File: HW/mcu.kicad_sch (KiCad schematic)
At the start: 10 parts, among them J2 JTAG, SW2 SW_DPST, SW3 SW_DPST, U1 ESP32-S2-MINI-2

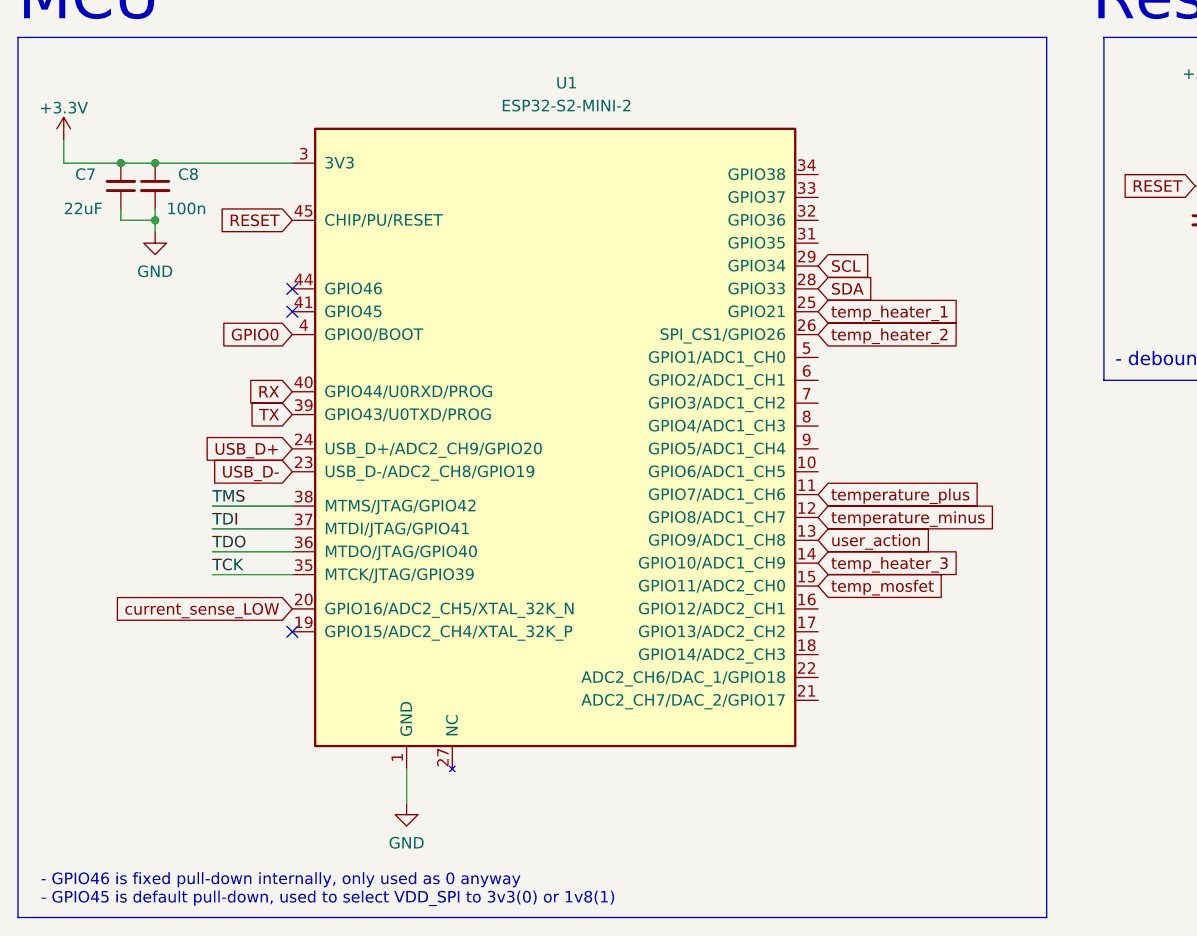
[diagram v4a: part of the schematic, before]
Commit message: starterd routing, removed OTG usb port
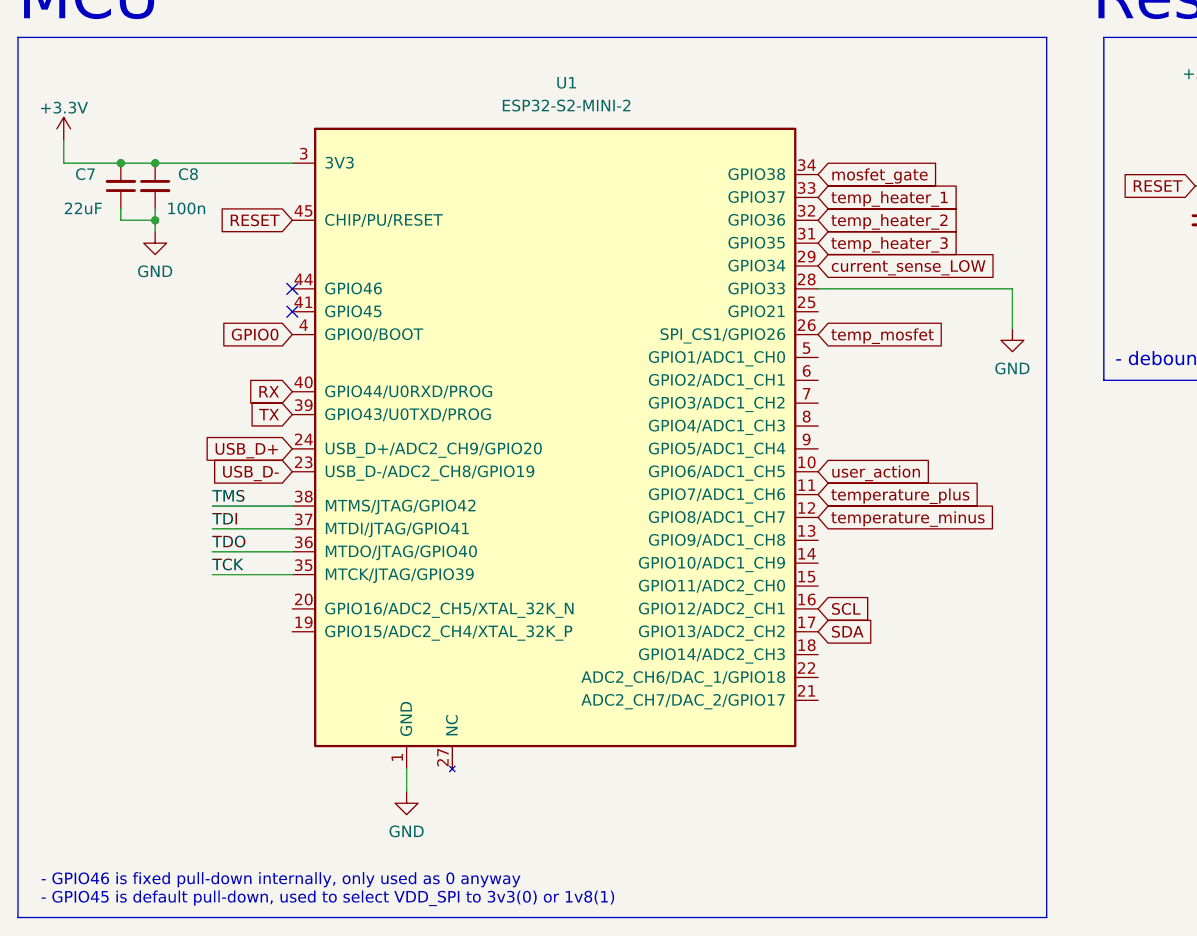
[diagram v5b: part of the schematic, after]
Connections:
- net GND: now also U1.2 (GND), U1.28 (GPIO33), U1.30 (GND), U1.42 (GND), U1.43 (GND), U1.46 (GND), U1.47 (GND), U1.48 (GND), U1.49 (GND), U1.50 (GND), U1.51 (GND), U1.52 (GND), U1.53 (GND), U1.54 (GND), U1.55 (GND), U1.56 (GND), U1.57 (GND), U1.58 (GND), U1.59 (GND), U1.60 (GND), U1.61 (GND), U1.62 (GND), U1.63 (GND), U1.64 (GND), U1.65 (GND)
- net SCL: now also U1.16 (GPIO12/ADC2_CH1); no longer U1.29 (GPIO34)
- net SDA: now also U1.17 (GPIO13/ADC2_CH2); no longer U1.28 (GPIO33)
- net current_sense_LOW: now also U1.29 (GPIO34); no longer U1.20 (GPIO16/ADC2_CH5/XTAL_32K_N)
- net temp_heater_1: now also U1.33 (GPIO37); no longer U1.25 (GPIO21)
- net temp_heater_2: now also U1.32 (GPIO36); no longer U1.26 (SPI_CS1/GPIO26)
- net temp_heater_3: now also U1.31 (GPIO35); no longer U1.14 (GPIO10/ADC1_CH9)
- net temp_mosfet: now also U1.26 (SPI_CS1/GPIO26); no longer U1.15 (GPIO11/ADC2_CH0)
- net user_action: now also U1.10 (GPIO6/ADC1_CH5); no longer U1.13 (GPIO9/ADC1_CH8)
- net mosfet_gate: now reaches U1.34 (GPIO38)
- no-connect marks 3 -> 2
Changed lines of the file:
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@@
   (no_connect (at 48.26 54.61))
   (no_connect (at 48.26 52.07))
-  (no_connect (at 48.26 90.17))
-  (wire (pts (xy 60.96 105.41) (xy 60.96 109.22))
+  (wire (pts (xy 60.96 105.41) (xy 60.96 107.95))
     (stroke (width 0) (type default) (color 0 0 0 0))
   )
@@
     (stroke (width 0) (type default) (color 0 0 0 0))
   )
+  (wire (pts (xy 106.68 52.07) (xy 128.27 52.07))
+    (stroke (width 0) (type default) (color 0 0 0 0))
+  )
   (wire (pts (xy 149.86 40.64) (xy 149.86 41.91))
     (stroke (width 0) (type default) (color 0 0 0 0))
@@
   )
   (wire (pts (xy 163.83 35.56) (xy 161.29 35.56))
+    (stroke (width 0) (type default) (color 0 0 0 0))
+  )
+  (wire (pts (xy 128.27 52.07) (xy 128.27 56.515))
     (stroke (width 0) (type default) (color 0 0 0 0))
   )
@@
     (effects (font (size 1.27 1.27)) (justify left bottom))
   )
-  (global_label "temp_heater_3" (shape input) (at 106.68 82.55 0) (fields_autoplaced)
-    (effects (font (size 1.27 1.27)) (justify left))
-    (property "Intersheet References" "${INTERSHEET_REFS}" (id 0) (at 122.8817 82.6294 0)
+  (global_label "temp_heater_3" (shape input) (at 106.68 46.99 0) (fields_autoplaced)
+    (effects (font (size 1.27 1.27)) (justify left))
+    (property "Intersheet References" "${INTERSHEET_REFS}" (id 0) (at 122.8817 47.0694 0)
       (effects (font (size 1.27 1.27)) (justify left) hide)
     )
@@
     )
   )
-  (global_label "user_action" (shape input) (at 106.68 80.01 0) (fields_autoplaced)
-    (effects (font (size 1.27 1.27)) (justify left))
-    (property "Intersheet References" "${INTERSHEET_REFS}" (id 0) (at 119.9788 80.0894 0)
+  (global_label "user_action" (shape input) (at 106.68 72.39 0) (fields_autoplaced)
+    (effects (font (size 1.27 1.27)) (justify left))
+    (property "Intersheet References" "${INTERSHEET_REFS}" (id 0) (at 119.9788 72.4694 0)
       (effects (font (size 1.27 1.27)) (justify left) hide)
     )
@@
     )
   )
-  (global_label "SDA" (shape input) (at 106.68 52.07 0) (fields_autoplaced)
-    (effects (font (size 1.27 1.27)) (justify left))
-    (property "Intersheet References" "${INTERSHEET_REFS}" (id 0) (at 112.6612 51.9906 0)
+  (global_label "SDA" (shape input) (at 106.68 90.17 0) (fields_autoplaced)
+    (effects (font (size 1.27 1.27)) (justify left))
+    (property "Intersheet References" "${INTERSHEET_REFS}" (id 0) (at 112.6612 90.0906 0)
       (effects (font (size 1.27 1.27)) (justify left) hide)
     )
@@
     )
   )
-  (global_label "temp_heater_1" (shape input) (at 106.68 54.61 0) (fields_autoplaced)
-    (effects (font (size 1.27 1.27)) (justify left))
-    (property "Intersheet References" "${INTERSHEET_REFS}" (id 0) (at 122.8817 54.6894 0)
-      (effects (font (size 1.27 1.27)) (justify left) hide)
-    )
-  )
-  (global_label "current_sense_LOW" (shape input) (at 48.26 87.63 180) (fields_autoplaced)
-    (effects (font (size 1.27 1.27)) (justify right))
-    (property "Intersheet References" "${INTERSHEET_REFS}" (id 0) (at 27.9459 87.7094 0)
-      (effects (font (size 1.27 1.27)) (justify right) hide)
+  (global_label "temp_heater_1" (shape input) (at 106.68 41.91 0) (fields_autoplaced)
+    (effects (font (size 1.27 1.27)) (justify left))
+    (property "Intersheet References" "${INTERSHEET_REFS}" (id 0) (at 122.8817 41.9894 0)
+      (effects (font (size 1.27 1.27)) (justify left) hide)
+    )
+  )
+  (global_label "mosfet_gate" (shape input) (at 106.68 39.37 0) (fields_autoplaced)
+    (effects (font (size 1.27 1.27)) (justify left))
+    (property "Intersheet References" "${INTERSHEET_REFS}" (id 0) (at 120.5836 39.4494 0)
+      (effects (font (size 1.27 1.27)) (justify left) hide)
+    )
+  )
+  (global_label "current_sense_LOW" (shape input) (at 106.68 49.53 0) (fields_autoplaced)
+    (effects (font (size 1.27 1.27)) (justify left))
+    (property "Intersheet References" "${INTERSHEET_REFS}" (id 0) (at 126.9941 49.4506 0)
+      (effects (font (size 1.27 1.27)) (justify left) hide)
     )
   )
@@
     )
   )
-  (global_label "temp_mosfet" (shape input) (at 106.68 85.09 0) (fields_autoplaced)
-    (effects (font (size 1.27 1.27)) (justify left))
-    (property "Intersheet References" "${INTERSHEET_REFS}" (id 0) (at 121.1279 85.1694 0)
+  (global_label "temp_mosfet" (shape input) (at 106.68 57.15 0) (fields_autoplaced)
+    (effects (font (size 1.27 1.27)) (justify left))
+    (property "Intersheet References" "${INTERSHEET_REFS}" (id 0) (at 121.1279 57.2294 0)
       (effects (font (size 1.27 1.27)) (justify left) hide)
     )
@@
     )
   )
-  (global_label "temp_heater_2" (shape input) (at 106.68 57.15 0) (fields_autoplaced)
-    (effects (font (size 1.27 1.27)) (justify left))
-    (property "Intersheet References" "${INTERSHEET_REFS}" (id 0) (at 122.8817 57.2294 0)
+  (global_label "temp_heater_2" (shape input) (at 106.68 44.45 0) (fields_autoplaced)
+    (effects (font (size 1.27 1.27)) (justify left))
+    (property "Intersheet References" "${INTERSHEET_REFS}" (id 0) (at 122.8817 44.5294 0)
       (effects (font (size 1.27 1.27)) (justify left) hide)
     )
@@
     )
   )
-  (global_label "SCL" (shape input) (at 106.68 49.53 0) (fields_autoplaced)
-    (effects (font (size 1.27 1.27)) (justify left))
-    (property "Intersheet References" "${INTERSHEET_REFS}" (id 0) (at 112.6007 49.4506 0)
+  (global_label "SCL" (shape input) (at 106.68 87.63 0) (fields_autoplaced)
+    (effects (font (size 1.27 1.27)) (justify left))
+    (property "Intersheet References" "${INTERSHEET_REFS}" (id 0) (at 112.6007 87.5506 0)
       (effects (font (size 1.27 1.27)) (justify left) hide)
     )
@@
     )
     (property "Datasheet" "" (id 3) (at 33.02 45.72 0)
+      (effects (font (size 1.27 1.27)) hide)
+    )
+    (pin "1")
+  )
+  (symbol (lib_id "power:GND") (at 128.27 56.515 0) (unit 1)
+    (in_bom yes) (on_board yes) (fields_autoplaced)
+    (property "Reference" "#PWR0129" (id 0) (at 128.27 62.865 0)
+      (effects (font (size 1.27 1.27)) hide)
+    )
+    (property "Value" "GND" (id 1) (at 128.27 60.9584 0))
+    (property "Footprint" "" (id 2) (at 128.27 56.515 0)
+      (effects (font (size 1.27 1.27)) hide)
+    )
+    (property "Datasheet" "" (id 3) (at 128.27 56.515 0)
       (effects (font (size 1.27 1.27)) hide)
     )
@@
     (pin "5")
   )
-  (symbol (lib_id "power:GND") (at 60.96 109.22 0) (unit 1)
+  (symbol (lib_id "power:GND") (at 60.96 107.95 0) (unit 1)
     (in_bom yes) (on_board yes) (fields_autoplaced)
-    (property "Reference" "#PWR0111" (id 0) (at 60.96 115.57 0)
-      (effects (font (size 1.27 1.27)) hide)
-    )
-    (property "Value" "GND" (id 1) (at 60.96 113.6634 0))
-    (property "Footprint" "" (id 2) (at 60.96 109.22 0)
-      (effects (font (size 1.27 1.27)) hide)
-    )
-    (property "Datasheet" "" (id 3) (at 60.96 109.22 0)
-      (effects (font (size 1.27 1.27)) hide)
-    )
+    (property "Reference" "#PWR0111" (id 0) (at 60.96 114.3 0)
+      (effects (font (size 1.27 1.27)) hide)
+    )
+    (property "Value" "GND" (id 1) (at 60.96 112.3934 0))
+    (property "Footprint" "" (id 2) (at 60.96 107.95 0)
+      (effects (font (size 1.27 1.27)) hide)
+    )
+    (property "Datasheet" "" (id 3) (at 60.96 107.95 0)
+      (effects (font (size 1.27 1.27)) hide)
+    )

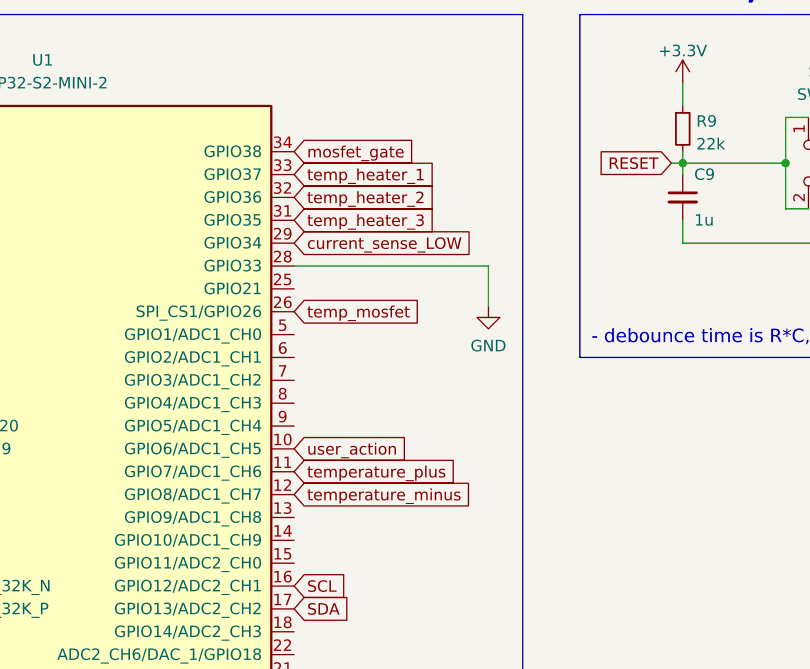
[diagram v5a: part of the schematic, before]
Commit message: Finished routing, only mosfet left, fixed layout, outline
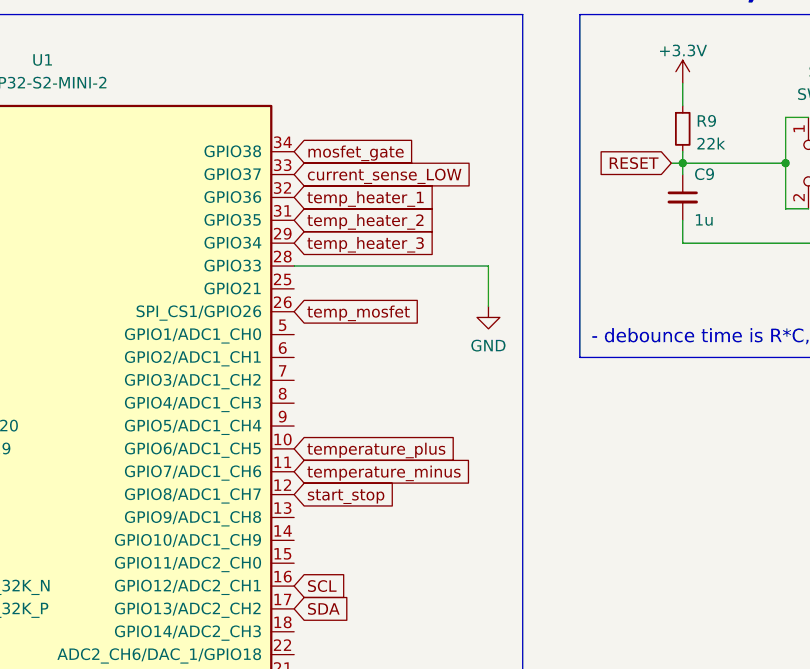
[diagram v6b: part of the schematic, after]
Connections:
- net user_action is gone; now on net temperature_plus: U1.10 (GPIO6/ADC1_CH5)
- net current_sense_LOW: now also U1.33 (GPIO37); no longer U1.29 (GPIO34)
- net temp_heater_1: now also U1.32 (GPIO36); no longer U1.33 (GPIO37)
- net temp_heater_2: now also U1.31 (GPIO35); no longer U1.32 (GPIO36)
- net temp_heater_3: now also U1.29 (GPIO34); no longer U1.31 (GPIO35)
- net temperature_minus: now also U1.11 (GPIO7/ADC1_CH6); no longer U1.12 (GPIO8/ADC1_CH7)
- net temperature_plus: no longer U1.11 (GPIO7/ADC1_CH6)
- new net start_stop: U1.12 (GPIO8/ADC1_CH7)
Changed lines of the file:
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@@
     (effects (font (size 1.27 1.27)) (justify left bottom))
   )
-  (global_label "temp_heater_3" (shape input) (at 106.68 46.99 0) (fields_autoplaced)
+  (global_label "temp_heater_3" (shape input) (at 106.68 49.53 0) (fields_autoplaced)
     (effects (font (size 1.27 1.27)) (justify left))
-    (property "Intersheet References" "${INTERSHEET_REFS}" (id 0) (at 122.8817 47.0694 0)
+    (property "Intersheet References" "${INTERSHEET_REFS}" (id 0) (at 122.8817 49.6094 0)
       (effects (font (size 1.27 1.27)) (justify left) hide)
     )
@@
     (property "Intersheet References" "${INTERSHEET_REFS}" (id 0) (at 40.1621 57.0706 0)
       (effects (font (size 1.27 1.27)) (justify right) hide)
-    )
-  )
-  (global_label "user_action" (shape input) (at 106.68 72.39 0) (fields_autoplaced)
-    (effects (font (size 1.27 1.27)) (justify left))
-    (property "Intersheet References" "${INTERSHEET_REFS}" (id 0) (at 119.9788 72.4694 0)
-      (effects (font (size 1.27 1.27)) (justify left) hide)
     )
   )
@@
     )
   )
-  (global_label "temp_heater_1" (shape input) (at 106.68 41.91 0) (fields_autoplaced)
+  (global_label "temp_heater_1" (shape input) (at 106.68 44.45 0) (fields_autoplaced)
     (effects (font (size 1.27 1.27)) (justify left))
-    (property "Intersheet References" "${INTERSHEET_REFS}" (id 0) (at 122.8817 41.9894 0)
+    (property "Intersheet References" "${INTERSHEET_REFS}" (id 0) (at 122.8817 44.5294 0)
       (effects (font (size 1.27 1.27)) (justify left) hide)
     )
@@
     )
   )
-  (global_label "current_sense_LOW" (shape input) (at 106.68 49.53 0) (fields_autoplaced)
+  (global_label "current_sense_LOW" (shape input) (at 106.68 41.91 0) (fields_autoplaced)
     (effects (font (size 1.27 1.27)) (justify left))
-    (property "Intersheet References" "${INTERSHEET_REFS}" (id 0) (at 126.9941 49.4506 0)
+    (property "Intersheet References" "${INTERSHEET_REFS}" (id 0) (at 126.9941 41.8306 0)
       (effects (font (size 1.27 1.27)) (justify left) hide)
     )
   )
-  (global_label "temperature_plus" (shape input) (at 106.68 74.93 0) (fields_autoplaced)
+  (global_label "temperature_plus" (shape input) (at 106.68 72.39 0) (fields_autoplaced)
     (effects (font (size 1.27 1.27)) (justify left))
-    (property "Intersheet References" "${INTERSHEET_REFS}" (id 0) (at 125.4821 75.0094 0)
+    (property "Intersheet References" "${INTERSHEET_REFS}" (id 0) (at 125.4821 72.4694 0)
       (effects (font (size 1.27 1.27)) (justify left) hide)
     )
@@
     )
   )
-  (global_label "temp_heater_2" (shape input) (at 106.68 44.45 0) (fields_autoplaced)
+  (global_label "temp_heater_2" (shape input) (at 106.68 46.99 0) (fields_autoplaced)
     (effects (font (size 1.27 1.27)) (justify left))
-    (property "Intersheet References" "${INTERSHEET_REFS}" (id 0) (at 122.8817 44.5294 0)
+    (property "Intersheet References" "${INTERSHEET_REFS}" (id 0) (at 122.8817 47.0694 0)
       (effects (font (size 1.27 1.27)) (justify left) hide)
     )
   )
-  (global_label "temperature_minus" (shape input) (at 106.68 77.47 0) (fields_autoplaced)
+  (global_label "start_stop" (shape input) (at 106.68 77.47 0) (fields_autoplaced)
     (effects (font (size 1.27 1.27)) (justify left))
-    (property "Intersheet References" "${INTERSHEET_REFS}" (id 0) (at 127.115 77.5494 0)
+    (property "Intersheet References" "${INTERSHEET_REFS}" (id 0) (at 118.5274 77.5494 0)
       (effects (font (size 1.27 1.27)) (justify left) hide)
     )
+  )
+  (global_label "temperature_minus" (shape input) (at 106.68 74.93 0) (fields_autoplaced)
+    (effects (font (size 1.27 1.27)) (justify left))
+    (property "Intersheet References" "${INTERSHEET_REFS}" (id 0) (at 127.115 75.0094 0)
+      (effects (font (size 1.27 1.27)) (justify left) hide)
+    )
